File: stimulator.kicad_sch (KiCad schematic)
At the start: 1 part, among them U1 ENS001-A2

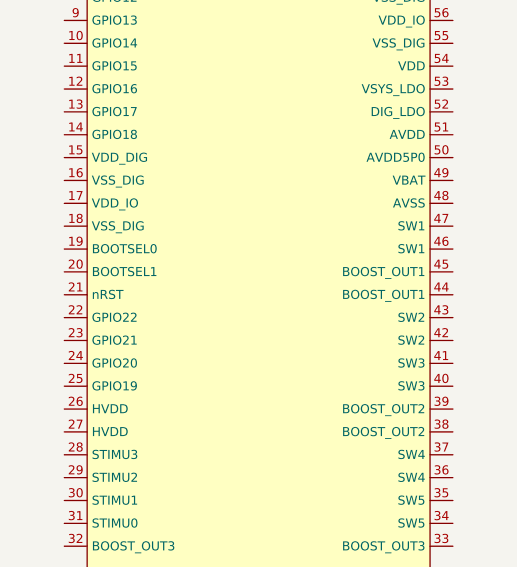
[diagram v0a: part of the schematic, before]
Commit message: esp32-s3 schematic adde
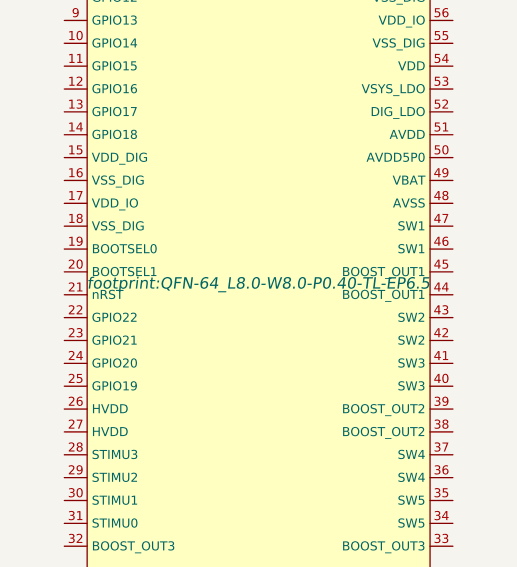
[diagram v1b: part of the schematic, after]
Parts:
- U1: distrubuter (none) -> jlcpcb
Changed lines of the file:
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@@
 		(property "Footprint" "footprint:QFN-64_L8.0-W8.0-P0.40-TL-EP6.5"
 			(at 120.65 99.06 0)
-			(hide yes)
 			(show_name no)
 			(do_not_autoplace no)
@@
 			(at 120.65 88.9 0)
 			(hide yes)
+			(show_name no)
+			(do_not_autoplace no)
+			(effects
+				(font
+					(size 1.27 1.27)
+				)
+			)
+		)
+		(property "distrubuter" "jlcpcb"
+			(at 120.65 88.9 0)
+			(hide yes)

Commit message: pin names assigned
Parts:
- added J1: Conn_01x06_Pin, symbol Connector:Conn_01x06_Pin
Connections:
- net +3V3: now reaches U1.17 (VDD_IO)
- net +3V3: now also U1.3 (VDD_IO), U1.56 (VDD_IO)
- net GNDD: now reaches U1.18 (VSS_DIG)
- net GNDD: now also U1.2 (VSS_DIG), U1.55 (VSS_DIG), U1.57 (VSS_DIG), U1.7 (VSS_DIG)
- net +1V8: now reaches U1.4 (VDD_DIG)
- net +1V8: now also U1.58 (VDD_DIG)
- net GNDA: now reaches U1.48 (AVSS)
- net vbat: now reaches U1.49 (VBAT)
- net swclk: now reaches U1.59 (GPIO0)
- net swdio: now reaches U1.60 (GPIO1)
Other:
- moved on the sheet: U1

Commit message: esp connected
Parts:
- removed J1: Conn_01x06_Pin, symbol Connector:Conn_01x06_Pin
- added J2: Conn_01x05_Pin, Connector_JST:JST_EH_B5B-EH-A_1x05_P2.50mm_Vertical, symbol Connector:Conn_01x05_Pin
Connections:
- net +3V3: now also J2.1 (Pin_1)
- net GNDD: now also J2.5 (Pin_5)
- net swclk: now also J2.3 (Pin_3)
- net swdio: now also J2.2 (Pin_2)
- net nrst: now reaches U1.21 (nRST)
- net nrst: now also J2.4 (Pin_4)
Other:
- note added: "Stimulator"

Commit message: peripherals added
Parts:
- added C1, C11, C13, C16, C3, C6, C7, C8: 100nF, Capacitor_SMD:C_0402_1005Metric, symbol Device:C
- added C10, C21, C54, C62, C64, C9: 10uF, Capacitor_SMD:C_0603_1608Metric, symbol Device:C
- added C12, C17: 4.7uF, Capacitor_SMD:C_0603_1608Metric, symbol Device:C
- added C15, C20, C4: 100uF, Capacitor_SMD:C_1206_3216Metric, symbol Device:C
- added C18: 27pF, Capacitor_SMD:C_0402_1005Metric, symbol Device:C
- added C19: 1nF, Capacitor_SMD:C_0402_1005Metric, symbol Device:C
- added C2: 4.7nF, Capacitor_SMD:C_0805_2012Metric, symbol Device:C
- added C22: 1uF, Capacitor_SMD:C_0603_1608Metric, symbol Device:C
- added C5: 1uF, Capacitor_SMD:C_0402_1005Metric, symbol Device:C
- added C63: 22pF, Capacitor_SMD:C_0402_1005Metric, symbol Device:C
- added D1: SK6812MINI, LED_SMD:LED_SK6812MINI_PLCC4_3.5x3.5mm_P1.75mm, symbol LED:SK6812MINI
- added D2: LED, LED_SMD:LED_1206_3216Metric, symbol Device:LED
- added D36: SS38, Diode_SMD:D_SMA, symbol Diode:MBRA340
- added F1: Fuse, Fuse:Fuse_1206_3216Metric, symbol Device:Fuse
- added F2: Fuse, Fuse:Fuse_1812_4532Metric, symbol Device:Fuse
- added H1, H2, H3, H4: MountingHole, MountingHole:MountingHole_2.2mm_M2, symbol Mechanical:MountingHole
- added J1: UART, KiCAD_Lib:P4_1.27mm_SMD, symbol Connector:Conn_01x04_Male
- added J10: Conn_01x05_Pin, KiCAD_Lib:HLK-LD2410C, symbol Connector:Conn_01x05_Pin
- added J11: Conn_01x03_Pin, KiCAD_Lib:EKMC1601111, symbol Connector:Conn_01x03_Pin
- added J3, J7: Conn_01x06_Pin, KiCAD_Lib:Conn_01x06_Pin, symbol Connector:Conn_01x06_Pin
- added J4: Micro_SD_Card, KiCAD_Lib:microSD_Card, symbol Connector:Micro_SD_Card
- added J5: Conn_01x02_Male, Battery:BatteryHolder_MPD_BH-18650-PC2, symbol StimulatorKiCad-rescue:Conn_01x02_Male-Connector
- added J6: TL3360, KiCAD_Lib:TL3360_Button, symbol Connector:Conn_01x02_Pin
- added J8: Conn_01x02_Male, KiCAD_Lib:Conn_1.27mm_2P, symbol StimulatorKiCad-rescue:Conn_01x02_Male-Connector
- added J9: KLS7-1290, NewLibrary:KLS7-MSS-1290CP, symbol StimulatorKiCad-rescue:Conn_01x02_Male-Connector
- added L1: ferrite, Inductor_SMD:L_0805_2012Metric, symbol Device:L
- added L2: 1277AS-H-4R7M=P2, Inductor_SMD:L_1210_3225Metric_Pad1.42x2.65mm_HandSolder, symbol StimulatorKiCad-rescue:1255AY-4R7M=P3-1255AY-4R7M_P3
- added L5: 1277AS-H-4R7M=P2, Inductor_SMD:L_1210_3225Metric_Pad1.42x2.65mm_HandSolder, symbol 1255AY-4R7M_P3:1255AY-4R7M=P3
- added P1: USB_C_Plug, Connector_USB:USB_C_Receptacle_HRO_TYPE-C-31-M-12, symbol Connector:USB_C_Plug
- added Q1: BSS138K, Package_TO_SOT_SMD:SOT-23, symbol Transistor_FET:IRLML2060
- added Q18, Q2, Q3, Q4: Si2301CDS, Package_TO_SOT_SMD:SOT-23, symbol Device:Q_PMOS_GSD
- added R1, R30: 1M, Resistor_SMD:R_0402_1005Metric, symbol Device:R
- added R10, R14, R18, R19, R2, R21, R22, R23, R24, R27, R28, R3, R5, R87, R88, R89, R90: 10k, Resistor_SMD:R_0402_1005Metric, symbol Device:R
- added R101, R25, R6, R94, R95: 100k, Resistor_SMD:R_0402_1005Metric, symbol Device:R
- added R103, R20, R29: 1k, Resistor_SMD:R_0402_1005Metric, symbol Device:R
- added R11: 0R, Resistor_SMD:R_0402_1005Metric, symbol Device:R
- added R12, R16, R17, R4, R9: 47k, Resistor_SMD:R_0402_1005Metric, symbol Device:R
- added R13: 0R, Resistor_SMD:R_0805_2012Metric, symbol Device:R
- added R15: 20k, Resistor_SMD:R_0402_1005Metric, symbol Device:R
- added R26: 75k, Resistor_SMD:R_0402_1005Metric, symbol Device:R
- added R31: 976k, Resistor_SMD:R_0402_1005Metric, symbol Device:R
- added R32: 309k, Resistor_SMD:R_0402_1005Metric, symbol Device:R
- added R7, R8: 5.1k, Resistor_SMD:R_0402_1005Metric, symbol Device:R
- added R85: 240k, Resistor_SMD:R_0402_1005Metric, symbol Device:R
- added R93: 430k, Resistor_SMD:R_0402_1005Metric, symbol Device:R
- added R96: 536k, Resistor_SMD:R_0402_1005Metric, symbol Device:R
- added U2: SMF05, KiCAD_Lib:SC-88, symbol New_Library:SMF05
- added U22, U23: LS0505, Package_DFN_QFN:DFN-8-1EP_2x2mm_P0.5mm_EP0.8x1.6mm, symbol New_Library:LS0505
- added U24: W25Q128JVS, Package_SON:WSON-8-1EP_6x5mm_P1.27mm_EP3.4x4mm, symbol Memory_Flash:W25Q128JVS
- added U25: MCP1725T, Package_DFN_QFN:DFN-8-1EP_3x2mm_P0.5mm_EP1.3x1.5mm, symbol Regulator_Linear:MCP1727-3302xMF
- added U3: MCP73855, Package_DFN_QFN:DFN-10-1EP_3x3mm_P0.5mm_EP1.55x2.48mm, symbol New_Library:MCP73855
- added U4: AP22653, Package_TO_SOT_SMD:SOT-23-6_Handsoldering, symbol New_Library:AP22653
- added U5: ESP32-S3-WROOM-1, KiCAD_Lib:ESP32-S3-WROOM-1, symbol New_Library:ESP32-S3-WROOM-1
- added U6: MCP1642D, Package_SO:MSOP-8-1EP_3x3mm_P0.65mm_EP1.68x1.88mm_ThermalVias, symbol StimulatorKiCad-rescue:MCP1642D-Regulator_Switching
- added U8: AP3401, KiCAD_Lib:DFN2020-6, symbol New_Library:AP3401
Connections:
- net +1V8: now also U1.15 (VDD_DIG), U1.54 (VDD)
- net GNDD: now also U1.16 (VSS_DIG)
- net nrst renamed Nrst
- net swclk renamed Swclk
- net swdio renamed Swdio
- net vbat renamed VBAT
- new net: Q2.1 (G), R20.2, R5.2
- new net: R88.2, R90.1, U24.3 (IO2)
- new net: R87.2, R89.1, U24.7 (IO3)
- new net: R30.1, U6.3 (PG)
- new net: R25.2, U25.5 (PWRGD)
- new net: C19.2, U25.6 (Cdelay)
- new net: R26.2, R27.1, U25.7 (Sense)
- new net: R11.1, U3.5 (PROG)
- new net: R13.1, U5.2 (3V3)
- new net: Q4.1 (G), R28.2, R29.2
- new net: R96.2, U22.7 (ILIM)
- new net: L5.1, U8.4 (LX)
- new net: P1.B5 (VCONN), R7.2
- new net: R18.2, U4.4 (FAULT)
- new net: R19.1, U4.5 (ILIM)
- new net: Q1.3 (D), R10.2, U3.10 (EN)
- new net: C11.1, U3.6 (TIMER)
- new net: L1.1, P1.A4 (VBUS), P1.A9 (VBUS), P1.B4 (VBUS), P1.B9 (VBUS)
- new net: P1.A5 (CC), R8.2
- new net: L2.1, U6.5 (SW)
- new net: J4.1 (DAT2), R16.2
- new net: Q3.3 (D), R23.1
- new net: C18.2, R31.1, R32.2, U6.2 (FB)
- new net: C63.2, R93.2, R94.1, U8.6 (FB)
- new net: J4.8 (DAT1), R4.2
- new net: R95.2, U8.2 (PG)
- new net: R85.2, U23.7 (ILIM)
- new net +5V: F1.2, L1.2, U2.1 (C1), U2.3 (C3), U2.4 (C4), U2.5 (C5), U2.6 (C6), U22.1 (IN), U22.5 (EN)
- new net AmbLight: C3.1, D2.1 (K), R3.2, U5.39 (IO1,ADC1_CH0)
- new net Batt_EN: Q3.1 (G), R21.2, R22.1, U5.25 (IO48)
- new net Batt_LVL: R23.2, R24.1, U5.38 (IO2,ADC1_CH1)
- new net Batt_Pos: C12.1, F2.1, J5.1 (Pin_1), J8.1 (Pin_1), U23.1 (IN), U23.5 (EN), U3.8 (VBAT1), U3.9 (VBAT2)
- new net Batt_Pos1: F2.2, Q18.3 (D), Q3.2 (S), R21.1, U23.8 (OUT)
- new net Button: C7.1, J6.1 (Pin_1), R2.2, U5.4 (IO4,ADC1_CH3)
- new net CE_En: Q1.1 (G), R103.2, U5.24 (IO47)
- new net ESP_EN: C5.1, R6.2, U5.3 (EN)
- new net FLASH_CS: U24.1 (~{CS}), U5.8 (IO15,ADC2_CH4,32K_P)
- new net GND: C1.2, C10.2, C11.2, C12.2, C13.2, C15.2, C16.2, C17.1, C19.1, C2.1, C20.2, C21.2, C22.1, C3.2, C4.2, C5.2, C54.2, C6.2, C62.1, C64.1, C7.2, C8.2, C9.2, D1.2 (VSS), J1.4 (Pin_4), J10.4 (Pin_4), J11.1 (Pin_1), J3.6 (Pin_6), J4.6 (VSS), J4.9 (SHIELD), J5.2 (Pin_2), J6.2 (Pin_2), J7.6 (Pin_6), J8.2 (Pin_2), P1.A1 (GND), P1.A12 (GND), P1.B1 (GND), P1.B12 (GND), Q1.2 (S), R1.2, R101.2, R103.1, R11.2, R15.2, R19.2, R22.2, R24.2, R27.2, R3.1, R32.1, R7.1, R8.1, R85.1, R89.2, R90.2, R94.2, R96.1, U2.2 (GND), U22.2 (GND), U22.9 (GND), U23.2 (GND), U23.9 (GND), U24.4 (GND), U25.4 (GND), U25.9 (GND), U3.11 (EP), U3.4 (VSS1), U3.7 (VSS2), U4.2 (GND), U5.1 (GND), U5.40 (GND), U5.41 (EPAD), U6.6 (Pgnd), U6.7 (Sgnd), U6.9 (Gnd), U8.5 (GND)
- new net IO0: J1.3 (Pin_3), U5.27 (IO0)
- new net MISO: J4.7 (DAT0), R9.2, U5.21 (IO13,ADC2_CH2)
- new net MOSI: J4.3 (CMD), R17.2, U5.19 (IO11,ADC2_CH0)
- new net NeoPixel: D1.3 (DIN), U5.31 (IO38)
- new net PIR: J11.2 (Pin_2), U5.15 (IO3,ADC1_CH2)
- new net Perip_EN: U5.13 (IO19,ADC2_CH8), U6.1 (EN)
- new net SCK: J4.5 (CLK), U5.20 (IO12,ADC2_CH1)
- new net SD_CS: J4.2 (DAT3/CD), R12.2, U5.14 (IO20,ADC2_CH9)
- new net SPI_CS: J3.5 (Pin_5), J7.5 (Pin_5), U5.17 (IO9,ADC1_CH8)
- new net SPI_MISO: J3.4 (Pin_4), J7.4 (Pin_4), U24.2 (DO(IO1)), U5.12 (IO8,ADC1_CH7)
- new net SPI_MOSI: J3.3 (Pin_3), J7.3 (Pin_3), U24.5 (DI(IO0)), U5.7 (IO7,ADC1_CH6)
- new net SPI_SCK: J3.2 (Pin_2), J7.2 (Pin_2), U24.6 (CLK), U5.6 (IO6,ADC1_CH5)
- new net SW1: C13.1, D36.1 (K), J9.1 (Pin_1), Q18.2 (S), U4.1 (IN)
- new net SW2: C15.1, C16.1, C17.2, C62.2, J9.2 (Pin_2), L2.2, Q2.2 (S), R5.1, R95.1, U25.1 (Vin), U25.2 (Vin), U25.3 (~{SHDN}), U4.6 (OUT), U6.8 (VIN), U8.1 (EN), U8.3 (VIN)
- new net Sensor_EN: R20.1, R29.1, U5.9 (IO16,ADC2_CH5,32K_N)
- new net Shield: C2.2, P1.S1 (SHIELD), R1.1
- new net U0RXD: J1.1 (Pin_1), U5.36 (IO44,U0RXD)
- new net U0TXD: J1.2 (Pin_2), U5.37 (IO43,U0TXD)
- new net USB_Voltage: R14.2, R15.1, U4.3 (EN), U5.18 (IO10,ADC1_CH9)
- new net VD: C18.1, C21.1, J10.5 (Pin_5), Q4.3 (D), R30.2, R31.2, U6.4 (Vout)
- new net VDD: C1.1, C20.1, C22.2, C4.1, C54.1, C6.1, C63.1, C64.2, C8.1, D1.4 (VDD), D2.2 (A), J11.3 (Pin_3), J4.4 (VDD), L5.2, Q4.2 (S), R12.1, R13.2, R16.1, R17.1, R2.1, R25.1, R26.1, R28.1, R4.1, R6.1, R87.1, R88.1, R9.1, R93.1, U24.8 (VCC), U25.8 (Vout)
- new net VUSB: D36.2 (A), F1.1, Q18.1 (G), R10.1, R101.1, R14.1, R18.1, U22.8 (OUT), U3.2 (VSET), U3.3 (VDD1)
- new net Vext: C10.1, C9.1, J3.1 (Pin_1), J7.1 (Pin_1), Q2.3 (D)
- new net mmWave_Out: J10.3 (Pin_3), U5.5 (IO5,ADC1_CH4)
- new net mmWave_RX: J10.2 (Pin_2), U5.10 (IO17,U1TXD,ADC2_CH6)
- new net mmWave_TX: J10.1 (Pin_1), U5.11 (IO18,U1RXD,ADC2_CH7)
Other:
- note added: "Ambient Light Sensor"
- note added: "Button"
- note added: "Connectors"
- note added: "Digital Supply"
- note added: "LED"
- note added: "Mechanicals"
- note added: "Memory"
- note added: "Microcontroller"
- note added: "PIR"
- note added: "USB & Battery Management"
- note added: "microSD"
- note added: "mmWave Radar"
- moved on the sheet: J2, U1

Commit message: schematic edits:deso
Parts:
- removed J10: Conn_01x05_Pin, KiCAD_Lib:HLK-LD2410C, symbol Connector:Conn_01x05_Pin
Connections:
- net VBAT is gone; now on net SW2: U1.49 (VBAT)
- net SW2: no longer C16.1, C17.2, C62.2, L2.2, Q2.2 (S), R5.1, R95.1, U25.1 (Vin), U25.2 (Vin), U25.3 (~{SHDN}), U6.8 (VIN), U8.1 (EN), U8.3 (VIN)
- new net Vbat: C16.1, C17.2, C62.2, L2.2, Q2.2 (S), R5.1, R95.1, U25.1 (Vin), U25.2 (Vin), U25.3 (~{SHDN}), U6.8 (VIN), U8.1 (EN), U8.3 (VIN)
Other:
- note removed: "mmWave Radar"
- moved on the sheet: H1, H2, H3, H4

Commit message: sch edit :novo
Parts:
- added D3: D_Schottky, symbol Device:D_Schottky
- added J10, J12, J13: Conn_01x02_Pin, symbol Connector:Conn_01x02_Pin
- added L3: 100uH, symbol Device:L
- added L4: 470uH, symbol Device:L
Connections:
- net SW2: now also L3.1, L4.1
- net at U1.26 (HVDD): now also U1.27 (HVDD), J13.1 (Pin_1)
- net BoostOut: now reaches U1.32 (BOOST_OUT3)
- net BoostOut: now also U1.33 (BOOST_OUT3), U1.38 (BOOST_OUT2), U1.39 (BOOST_OUT2), U1.44 (BOOST_OUT1), U1.45 (BOOST_OUT1), D3.1 (K), J13.2 (Pin_2)
- net Sw: now reaches U1.34 (SW5)
- net Sw: now also U1.35 (SW5), U1.36 (SW4), U1.37 (SW4), U1.40 (SW3), U1.41 (SW3), U1.42 (SW2), U1.43 (SW2), U1.46 (SW1), U1.47 (SW1), D3.2 (A), J10.2 (Pin_2), J12.2 (Pin_2)
- new net: J12.1 (Pin_1), L4.2
- new net: J10.1 (Pin_1), L3.2
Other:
- moved on the sheet: J2, U1
